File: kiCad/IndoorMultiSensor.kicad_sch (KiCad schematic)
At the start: 7 parts, among them U2 Pico

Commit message: CAD schematics completed.
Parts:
- added C1: 220uF, symbol Device:C
- added D1: 1N4148WT, Diode_SMD:D_SOD-523, symbol Diode:1N4148WT
- added MK1: Microphone_Condenser, symbol Device:Microphone_Condenser
- added R5: 200Ω, symbol Device:R
- added SW1: SW_DPST_x2, symbol Switch:SW_DPST_x2
- added U1: BME280, Package_LGA:Bosch_LGA-8_2.5x2.5mm_P0.65mm_ClockwisePinNumbering, symbol Sensor:BME280
- added U3: RX8900, symbol Timer_RTC:RX8901CE
- added U4: MHZ19C, symbol Timer_RTC:RX8901CE
- renumbered 16×2行 to LCD1, 16×2行1 to LCD2
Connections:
- net at LCD1.2 (VDD), LCD2.2 (VDD), R1.1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: now also C1.1, U1.1 (VDD), U4.4 (Vin)
- net at U2.16 (GPIO12): now also U4.5 (R_{X})
- net at U2.17 (GPIO13): now also U4.6 (T_{X})
- net at U2.31 (GPIO26_ADC0): now also U1.4 (SDI)
- net at U2.32 (GPIO27_ADC1): now also U1.6 (SCK)
- net at U2.36 (3V3): now also U3.8 (V_{DD})
- net at U2.38 (GND): now also C1.2, SW1.2 (B), U1.2 (GND), U1.5 (SDO), U4.3 (GND)
- net at U2.6 (GPIO4): now also U3.6 (SDA)
- net at U2.7 (GPIO5): now also U3.5 (SCL)
- net at U2.8 (GND): now also D1.1 (K), MK1.1 (-), U3.4 (GND)
- new net: SW1.1 (A), U4.1 (HD)
- new net: D1.2 (A), MK1.2 (+), R5.1
- new net: R5.2, U3.7 (V_{BAT})
- no-connect marks 8 -> 14
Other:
- note added: "Short J3"
- moved on the sheet: LCD1, LCD2, U2

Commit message: Modified CAD appearance.
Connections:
- net at C1.2, SW1.2 (B), U4.3 (GND): now also U2.28 (GND); no longer U1.2 (GND), U1.5 (SDO), U2.38 (GND)
- new net: U1.2 (GND), U1.5 (SDO), U2.38 (GND)
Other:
- title: (none) -> IndoorMultiSensor
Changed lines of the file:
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@@
 	(generator_version "8.0")
 	(paper "A4")
+	(title_block
+		(title "IndoorMultiSensor")
+		(date "2024-09-15")
+		(rev "1.0.0")
+	)
 	(junction
 		(at 119.38 64.77)
@@
 	)
 	(junction
-		(at 209.55 66.04)
+		(at 119.38 135.89)
 		(diameter 0)
-		(color 0 0 0 1)
+		(color 255 0 0 1)
 	)
 	(junction
@@
 	)
 	(junction
+		(at 209.55 105.41)
+		(diameter 0)
+		(color 0 0 0 1)
+	)
+	(junction
 		(at 209.55 58.42)
 		(diameter 0)
@@
 		(at 121.92 72.39)
 		(diameter 0)
-		(color 0 0 0 0)
+		(color 0 0 0 1)
 	)
 	(junction
@@
 	)
 	(junction
-		(at 209.55 104.14)
-		(diameter 0)
-		(color 0 0 0 1)
-	)
-	(junction
 		(at 148.59 49.53)
 		(diameter 0)
@@
 		(color 0 0 0 1)
 	)
-	(junction
-		(at 116.84 135.89)
-		(diameter 0)
-		(color 255 0 0 1)
-	)
 	(no_connect
 		(at 97.79 80.01)
@@
 	(wire
 		(pts
-			(xy 207.01 35.56) (xy 207.01 48.26)
+			(xy 207.01 38.1) (xy 207.01 48.26)
 		)
 		(stroke
@@
 	(wire
 		(pts
-			(xy 87.63 38.1) (xy 87.63 80.01)
+			(xy 87.63 39.37) (xy 87.63 80.01)
 		)
 		(stroke
@@
 	(wire
 		(pts
-			(xy 170.18 121.92) (xy 170.18 104.14)
+			(xy 170.18 121.92) (xy 170.18 105.41)
 		)
 		(stroke
@@
 	(wire
 		(pts
-			(xy 170.18 104.14) (xy 182.88 104.14)
+			(xy 170.18 105.41) (xy 182.88 105.41)
 		)
 		(stroke
@@
 	(wire
 		(pts
-			(xy 193.04 104.14) (xy 209.55 104.14)
+			(xy 193.04 105.41) (xy 209.55 105.41)
+		)
+		(stroke
+			(width 0)
+			(type default)
+			(color 0 0 0 1)
+		)
+	)
+	(wire
+		(pts
+			(xy 209.55 105.41) (xy 209.55 114.3)
 		)
 		(stroke
@@
 	(wire
 		(pts
-			(xy 119.38 35.56) (xy 119.38 64.77)
+			(xy 119.38 38.1) (xy 119.38 64.77)
 		)
 		(stroke
@@
 	(wire
 		(pts
-			(xy 168.91 43.18) (xy 168.91 53.34)
+			(xy 168.91 41.91) (xy 168.91 53.34)
+		)
+		(stroke
+			(width 0)
+			(type default)
+			(color 0 0 0 1)
+		)
+	)
+	(wire
+		(pts
+			(xy 209.55 78.74) (xy 207.01 78.74)
 		)
 		(stroke
@@
 	(wire
 		(pts
-			(xy 119.38 35.56) (xy 207.01 35.56)
+			(xy 119.38 38.1) (xy 207.01 38.1)
 		)
 		(stroke
@@
 	(wire
 		(pts
-			(xy 119.38 135.89) (xy 116.84 135.89)
-		)
-		(stroke
-			(width 0)
-			(type default)
-			(color 255 0 0 1)
-		)
-	)
-	(wire
-		(pts
 			(xy 217.17 111.76) (xy 217.17 114.3)
 		)
@@
 	(wire
 		(pts
-			(xy 121.92 43.18) (xy 168.91 43.18)
+			(xy 121.92 41.91) (xy 168.91 41.91)
 		)
 		(stroke
@@
 	(wire
 		(pts
+			(xy 119.38 139.7) (xy 116.84 139.7)
+		)
+		(stroke
+			(width 0)
+			(type default)
+			(color 255 0 0 1)
+		)
+	)
+	(wire
+		(pts
 			(xy 207.01 53.34) (xy 209.55 53.34)
 		)
@@
 	(wire
 		(pts
-			(xy 171.45 38.1) (xy 171.45 48.26)
-		)
-		(stroke
-			(width 0)
-			(type default)
-		)
-	)
-	(wire
-		(pts
-			(xy 87.63 38.1) (xy 171.45 38.1)
+			(xy 171.45 39.37) (xy 171.45 48.26)
+		)
+		(stroke
+			(width 0)
+			(type default)
+		)
+	)
+	(wire
+		(pts
+			(xy 87.63 39.37) (xy 171.45 39.37)
 		)
 		(stroke
@@
 	(wire
 		(pts
-			(xy 77.47 135.89) (xy 116.84 135.89)
+			(xy 77.47 135.89) (xy 119.38 135.89)
 		)
 		(stroke
@@
 	(wire
 		(pts
-			(xy 209.55 66.04) (xy 209.55 104.14)
-		)
-		(stroke
-			(width 0)
-			(type default)
-			(color 0 0 0 1)
-		)
-	)
-	(wire
-		(pts
 			(xy 105.41 144.78) (xy 232.41 144.78)
 		)
@@
 	(wire
 		(pts
-			(xy 209.55 104.14) (xy 209.55 114.3)
+			(xy 209.55 78.74) (xy 209.55 105.41)
 		)
 		(stroke
@@
 	(wire
 		(pts
-			(xy 116.84 135.89) (xy 116.84 139.7)
+			(xy 119.38 135.89) (xy 119.38 139.7)
 		)
 		(stroke
@@
 	(wire
 		(pts
-			(xy 121.92 43.18) (xy 121.92 72.39)
+			(xy 121.92 41.91) (xy 121.92 72.39)
 		)
 		(stroke
@@
 	(symbol
 		(lib_id "Switch:SW_DPST_x2")
-		(at 187.96 104.14 0)
+		(at 187.96 105.41 0)
 		(unit 1)
 		(exclude_from_sim no)
@@
 		(fields_autoplaced yes)
 		(property "Reference" "SW1"
-			(at 187.96 100.33 0)
+			(at 187.96 101.6 0)
 			(effects
 				(font
@@
 		)
 		(property "Value" "SW_DPST_x2"
-			(at 187.96 100.33 0)
+			(at 187.96 101.6 0)
 			(effects
 				(font
@@
 		)
 		(property "Footprint" ""
-			(at 187.96 104.14 0)
+			(at 187.96 105.41 0)
 			(effects
 				(font
@@
 		)
 		(property "Datasheet" "~"
-			(at 187.96 104.14 0)
+			(at 187.96 105.41 0)
 			(effects
 				(font
@@
 		)
 		(property "Description" "Single Pole Single Throw (SPST) switch, separate symbol"
-			(at 187.96 104.14 0)
-			(effects
-				(font
+			(at 187.96 105.41 0)
+			(effects
+				(font

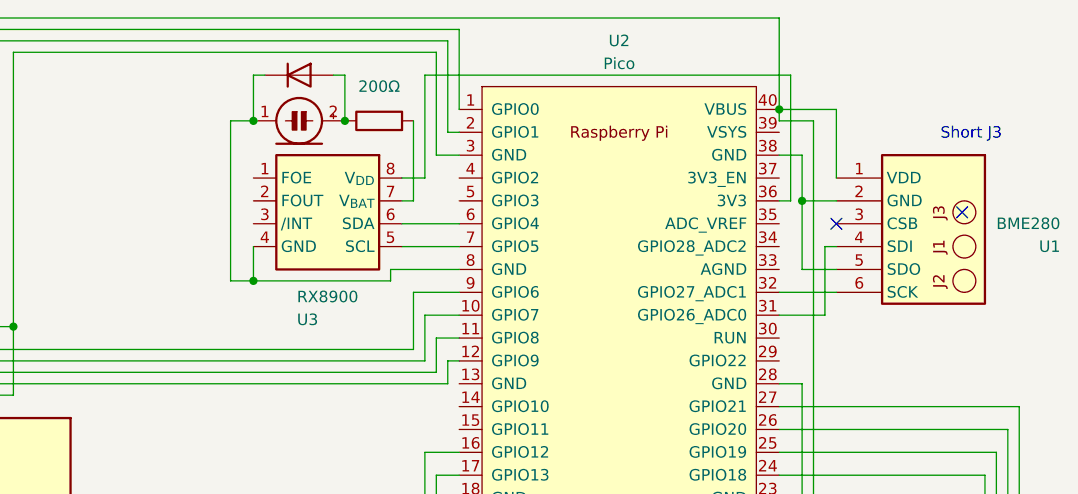
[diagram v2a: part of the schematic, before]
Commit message: fixed footprint symbols
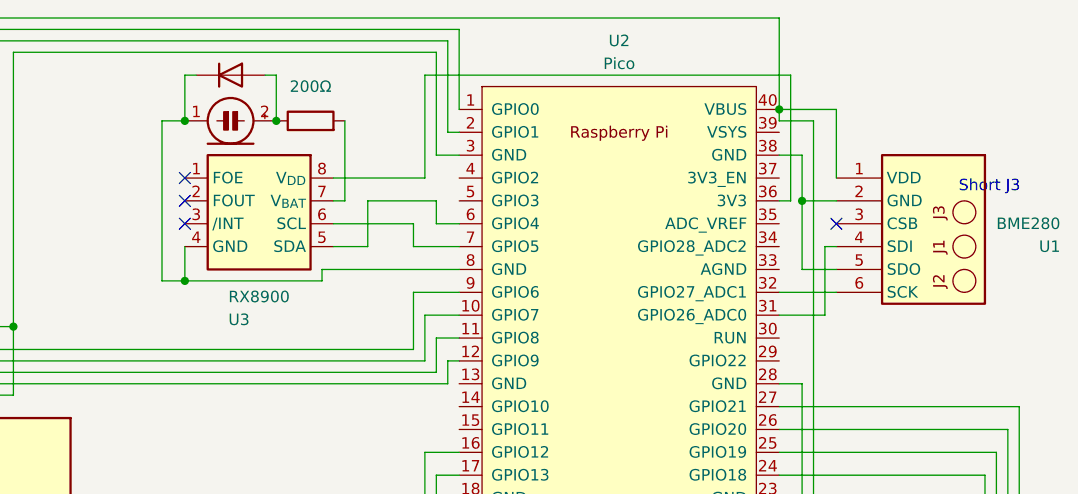
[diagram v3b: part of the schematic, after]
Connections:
- net at U2.6 (GPIO4): now also U3.5 (SDA); no longer U3.6 (SDA)
- net at U2.7 (GPIO5): now also U3.6 (SCL); no longer U3.5 (SCL)
- no-connect marks 14 -> 16
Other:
- moved on the sheet: U3
